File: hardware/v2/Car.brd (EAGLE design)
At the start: 83.8 x 55.9 mm, 64 parts

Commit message: Fixed PGD/PGC error (swapped) in schematic.
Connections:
- net N$28: now also ICD.5; no longer ICD.4
- net N$3: now also ICD.4; no longer ICD.5
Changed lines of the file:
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@@
 <?xml version="1.0" encoding="utf-8"?>
 <!DOCTYPE eagle SYSTEM "eagle.dtd">
-<eagle version="7.1.0">
+<eagle version="7.2.0">
 <drawing>
 <settings>
@@
 <signal name="N$3">
 <contactref element="BRAINS" pad="4"/>
-<contactref element="ICD" pad="5"/>
-<wire x1="2.032" y1="7.62" x2="38.1" y2="32.72" width="0" layer="19" extent="1-1"/>
+<contactref element="ICD" pad="4"/>
+<wire x1="1.778" y1="10.16" x2="38.1" y2="32.72" width="0" layer="19" extent="1-1"/>
 </signal>
 <signal name="N$28">
 <contactref element="BRAINS" pad="5"/>
-<contactref element="ICD" pad="4"/>
-<wire x1="1.778" y1="10.16" x2="36.83" y2="32.72" width="0" layer="19" extent="1-1"/>
+<contactref element="ICD" pad="5"/>
+<wire x1="2.032" y1="7.62" x2="36.83" y2="32.72" width="0" layer="19" extent="1-1"/>
 </signal>
 <signal name="N$30">

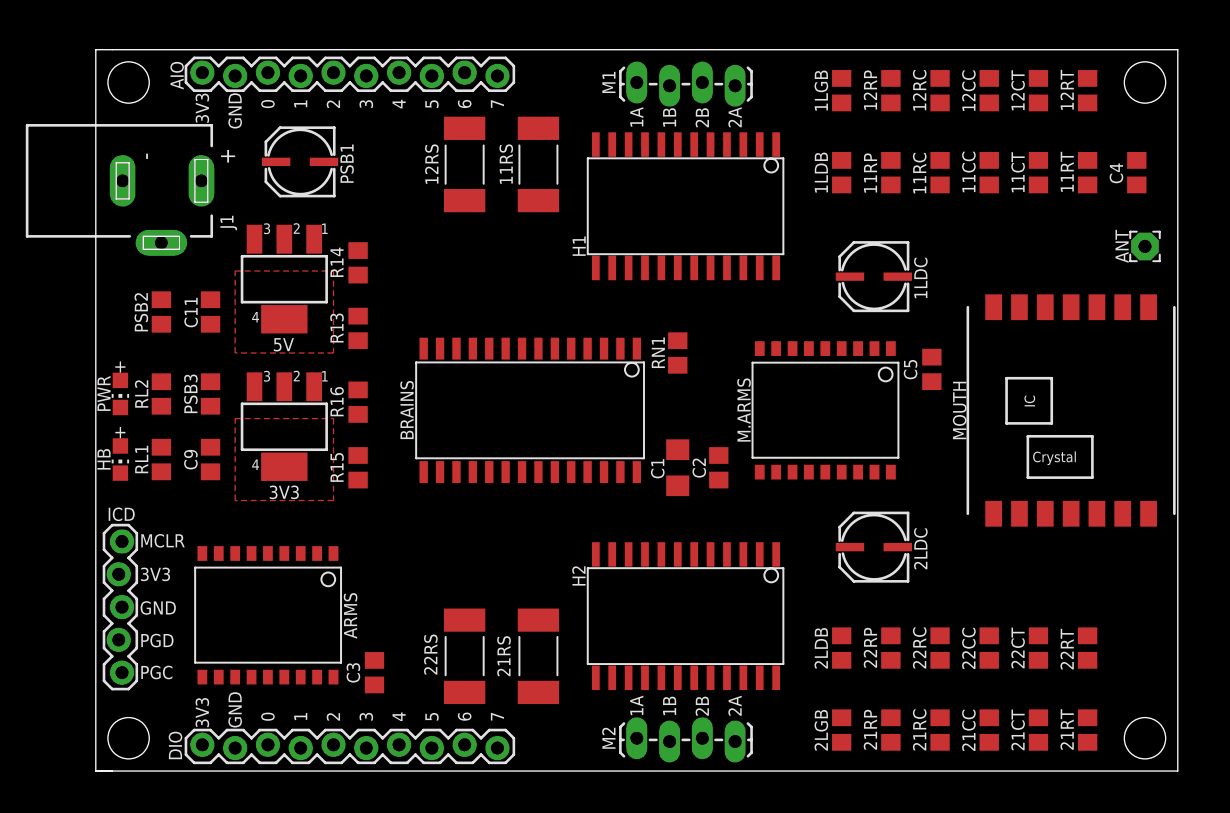
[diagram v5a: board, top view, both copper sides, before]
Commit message: Swapped non-analog input pins for ones that do support analog input. Significantly cleaned up schematic.
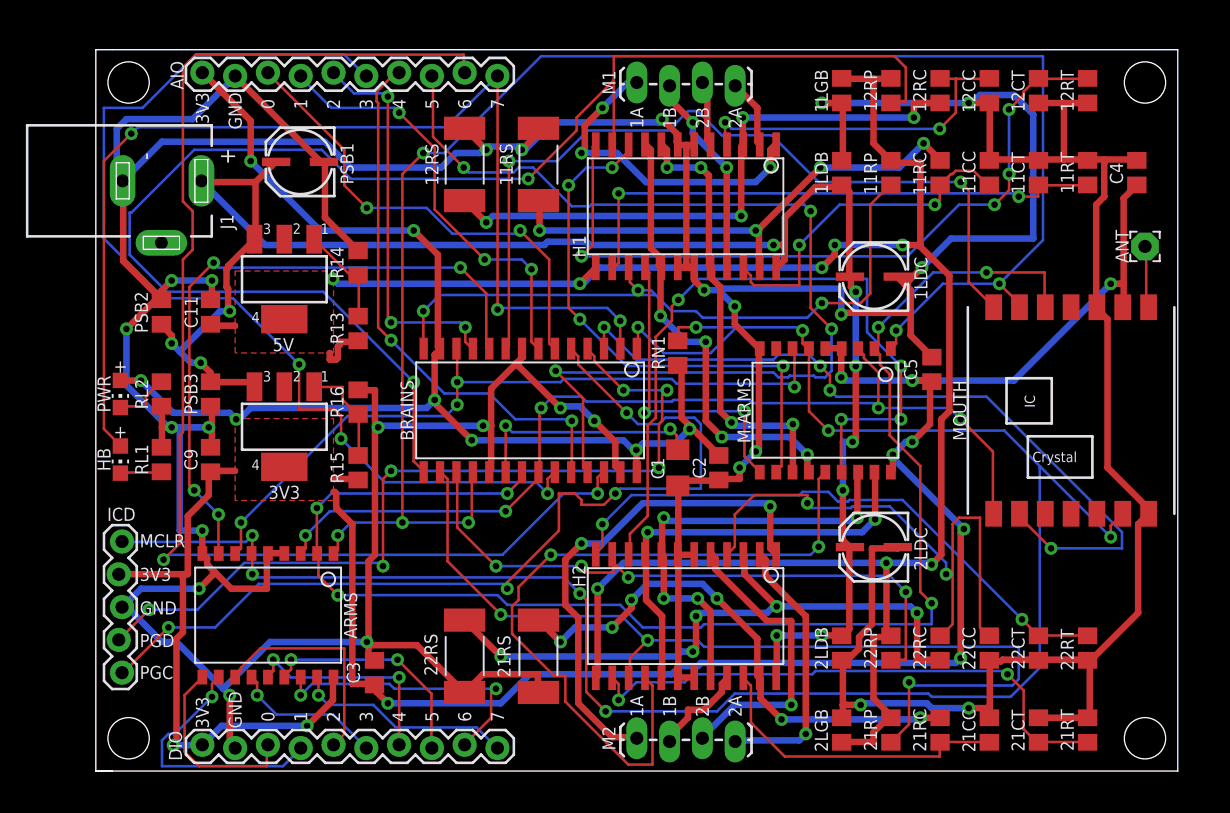
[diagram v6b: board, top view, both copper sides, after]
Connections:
- net N$12 renamed D0
- net N$19 renamed M2_V2
- net N$21 renamed M1_V2
- net N$23 renamed M1_I0X
- net N$25 renamed MOSI
- net N$26 renamed MISO
- net N$28 renamed PGC
- net N$3 renamed PGD
- net N$30 renamed M1_V1
- net N$38 renamed M2_V1
- net N$39 renamed D1
- net N$43 renamed D2
- net N$44 renamed D3
- net N$47 renamed D4
- net N$48 renamed D5
- net N$49 renamed D6
- net N$50 renamed D7
- net N$56 renamed M1_I1X
- net N$60 renamed M2_I0X
- net N$61 renamed M2_I1X
- net N$62 renamed M1_P1
- net N$63 renamed M1_P2
- net N$66 renamed M2_P1
- net N$67 renamed M2_P2
- net N$7 renamed SCLK
- net VCCIO renamed /RST
- removed net N$22: BRAINS.25, MOUTH.14
- removed net N$24: BRAINS.26, MOUTH.2
- removed net N$29: AIO.5, BRAINS.9
- removed net N$32: AIO.6, BRAINS.10
- removed net N$36: ARMS.7, BRAINS.23, M.ARMS.7
- removed net N$37: ARMS.8, BRAINS.24
- removed net N$45: AIO.3, BRAINS.2, HB.A
- removed net N$53: AIO.4, BRAINS.3
- removed net N$54: AIO.8, BRAINS.6
- removed net N$55: AIO.9, BRAINS.7
- removed net N$57: AIO.7, BRAINS.12
- removed net N$59: AIO.10, BRAINS.11
- new net A0: AIO.3, BRAINS.6
- new net A1: AIO.4, BRAINS.7
- new net A2: AIO.5, BRAINS.11
- new net A3: AIO.6, BRAINS.23
- new net A4: AIO.7, BRAINS.24
- new net A5: AIO.8, BRAINS.25
- new net A6: AIO.9, BRAINS.26
- new net A7: AIO.10, BRAINS.2, HB.A
- new net DIO_CS: ARMS.7, BRAINS.12, M.ARMS.7
- new net DIO_IRQ: ARMS.8, BRAINS.10
- new net RFM_CS: BRAINS.9, MOUTH.14
- new net RFM_IRQ: BRAINS.3, MOUTH.2
- net +3V3: now also PWR.A
- net +5V: no longer PWR.A
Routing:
- net GND: track 0.00 -> 497.1 mm, vias 0 -> 26
- net +3V3: track 0.00 -> 274.8 mm, vias 0 -> 18
- net /RST: track 0.00 -> 158.0 mm, vias 0 -> 9
- net +5V: track 0.00 -> 153.5 mm, vias 0 -> 8
- net +12V: track 0.00 -> 135.1 mm, vias 0 -> 10
- net SCLK: track 0.00 -> 129.1 mm, vias 0 -> 6
- net M1_V2: track 0.00 -> 114.6 mm, vias 0 -> 2
- net MOSI: track 0.00 -> 114.2 mm, vias 0 -> 6
- net A6: track 0.00 -> 100.6 mm, vias 0 -> 2
- net A7: track 0.00 -> 86.0 mm, vias 0 -> 3
- net A5: track 0.00 -> 80.6 mm, vias 0 -> 4
- net A3: track 0.00 -> 80.4 mm, vias 0 -> 3
- net MISO: track 0.00 -> 74.3 mm, vias 0 -> 5
- net M2_V1: track 0.00 -> 74.3 mm, vias 0 -> 3
- net PGC: track 0.00 -> 72.2 mm, vias 0 -> 4
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
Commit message: More schematic and layout cleanup.
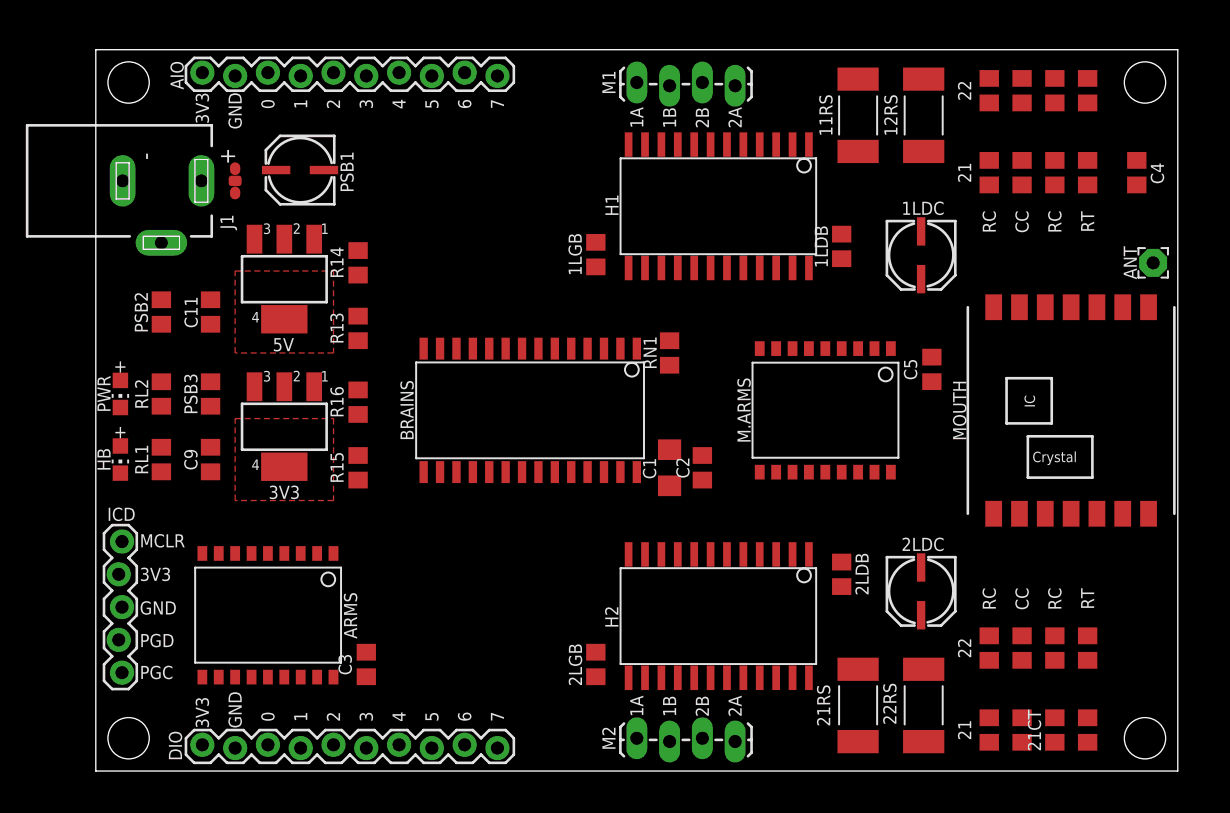
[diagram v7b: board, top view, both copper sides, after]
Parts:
- removed 11RP, 12RP, 21RP, 22RP: 10k, rcl:R0805
- added JMP1: 0R-JUMPC, jump-0r-smd:C0R-JMP
- 11CC, 11CT, 12CC, 12CT, 21CC, 21CT, 22CC, 22CT: value 820p -> 1n
- 11RC, 12RC, 21RC, 22RC: value 1k -> 2k
- 11RT, 12RT, 21RT, 22RT: value 56k -> 22k
- moved 12RS 35.8 mm to (64.1, 50.8)
- moved 22RS 35.8 mm to (64.1, 5.08)
- moved 11RS 25.1 mm to (59.1, 50.8)
- moved 21RS 25.1 mm to (59.1, 5.08)
- moved 1LGB 22.9 mm to (38.7, 40.0), turned to 90 degrees
- moved 2LGB 19.7 mm to (38.7, 8.26)
- moved 2LDB 5.71 mm to (57.8, 15.2), turned to 90 degrees
- moved 1LDB 5.71 mm to (57.8, 40.6)
- moved 2LDC 4.96 mm to (64.1, 14.0), turned to 270 degrees
- moved 1LDC 4.26 mm to (64.1, 40.0), turned to 270 degrees
- moved 11RC 3.81 mm to (69.2, 46.4)
- moved 12RC 3.81 mm to (69.2, 52.7)
- moved 21RC 3.81 mm to (69.2, 3.17)
- moved 22RC 3.81 mm to (69.2, 9.53)
- moved H1 2.54 mm to (48.3, 43.8)
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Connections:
- net +12V renamed 12V
- net +3V3 renamed 3V3
- removed net +5V: 11RP.2, 12RP.2, 1LGB.1, 21RP.2, 22RP.2, 2LGB.1, 5V.4, C11.1, H1.13, H2.13, R13.2
- new net 5V: 1LGB.1, 2LGB.1, 5V.4, C11.1, H1.13, H2.13, R13.2
- new net AGND: 11CC.2, 11CT.2, 11RS.1, 11RT.1, 12CC.2, 12CT.2, 12RS.1, 12RT.1, 1LDB.2, 1LDC.-, 21CC.2, 21CT.2, 21RS.1, 21RT.1, 22CC.2, 22CT.2, 22RS.1, 22RT.1, 2LDB.2, 2LDC.-, JMP1.3
- new net DGND: 1LGB.2, 2LGB.2, AIO.2, ARMS.4, ARMS.5, ARMS.9, BRAINS.19, BRAINS.27, BRAINS.8, C1.2, C2.2, C3.2, C4.2, C5.2, DIO.2, H1.18, H1.19, H1.6, H1.7, H2.18, H2.19, H2.6, H2.7, ICD.3, JMP1.1, M.ARMS.9, MOUTH.10, MOUTH.7, RL1.2
- net GND: now also JMP1.2; no longer 11CC.2, 11CT.2, 11RS.1, 11RT.1, 12CC.2, 12CT.2, 12RS.1, 12RT.1, 1LDB.2, 1LDC.-, 1LGB.2, 21CC.2, 21CT.2, 21RS.1, 21RT.1, 22CC.2, 22CT.2, 22RS.1, 22RT.1, 2LDB.2, 2LDC.-, 2LGB.2, AIO.2, ARMS.4, ARMS.5, ARMS.9, BRAINS.19, BRAINS.27, BRAINS.8, C1.2, C2.2, C3.2, C4.2, C5.2, DIO.2, H1.18, H1.19, H1.6, H1.7, H2.18, H2.19, H2.6, H2.7, ICD.3, M.ARMS.9, MOUTH.10, MOUTH.7, RL1.2
- net M1_V1: no longer 11RP.1
- net M1_V2: no longer 12RP.1
- net M2_V1: no longer 21RP.1
- net M2_V2: no longer 22RP.1
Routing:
- net GND: track 497.1 -> 0.00 mm, vias 26 -> 0
- net 3V3: track 274.8 -> 0.00 mm, vias 18 -> 0
- net /RST: track 158.0 -> 0.00 mm, vias 9 -> 0
- net +5V: track 153.5 -> 0.00 mm, vias 8 -> 0
- net 12V: track 135.1 -> 0.00 mm, vias 10 -> 0
- net SCLK: track 129.1 -> 0.00 mm, vias 6 -> 0
- net M1_V2: track 114.6 -> 0.00 mm, vias 2 -> 0
- net MOSI: track 114.2 -> 0.00 mm, vias 6 -> 0
- net A6: track 100.6 -> 0.00 mm, vias 2 -> 0
- net A7: track 86.0 -> 0.00 mm, vias 3 -> 0
- net A5: track 80.6 -> 0.00 mm, vias 4 -> 0
- net A3: track 80.4 -> 0.00 mm, vias 3 -> 0
- net MISO: track 74.3 -> 0.00 mm, vias 5 -> 0
- net M2_V1: track 74.3 -> 0.00 mm, vias 3 -> 0
- net PGC: track 72.2 -> 0.00 mm, vias 4 -> 0
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- added copper zone on layer 1, net +3V3
- removed copper zone on layer 1, net 3V3
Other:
- outline, holes or cut-outs redrawn
- board text added: "21"
- board text added: "22"
- board text added: "CC"
- board text added: "RC"
- board text added: "RT"

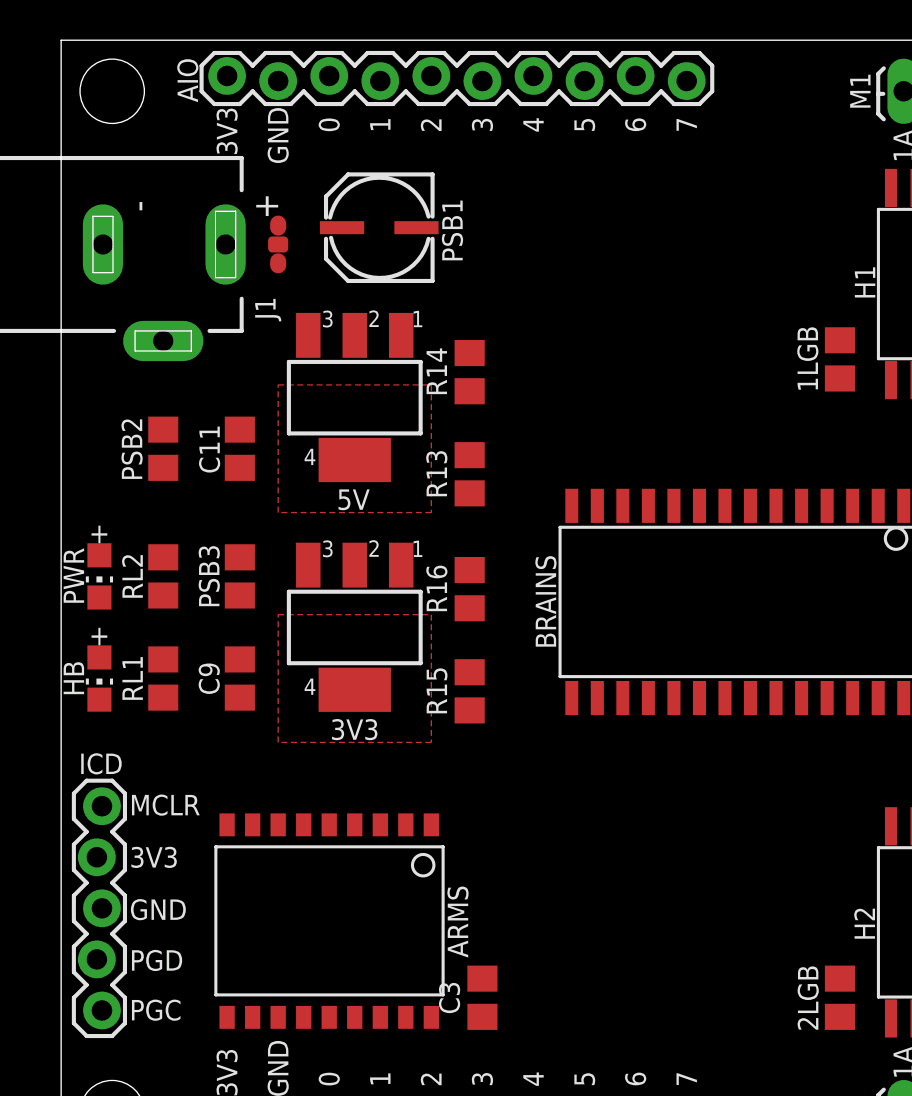
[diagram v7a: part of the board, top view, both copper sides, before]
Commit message: Adding low pass filters to PWM outputs (for motor VREF).
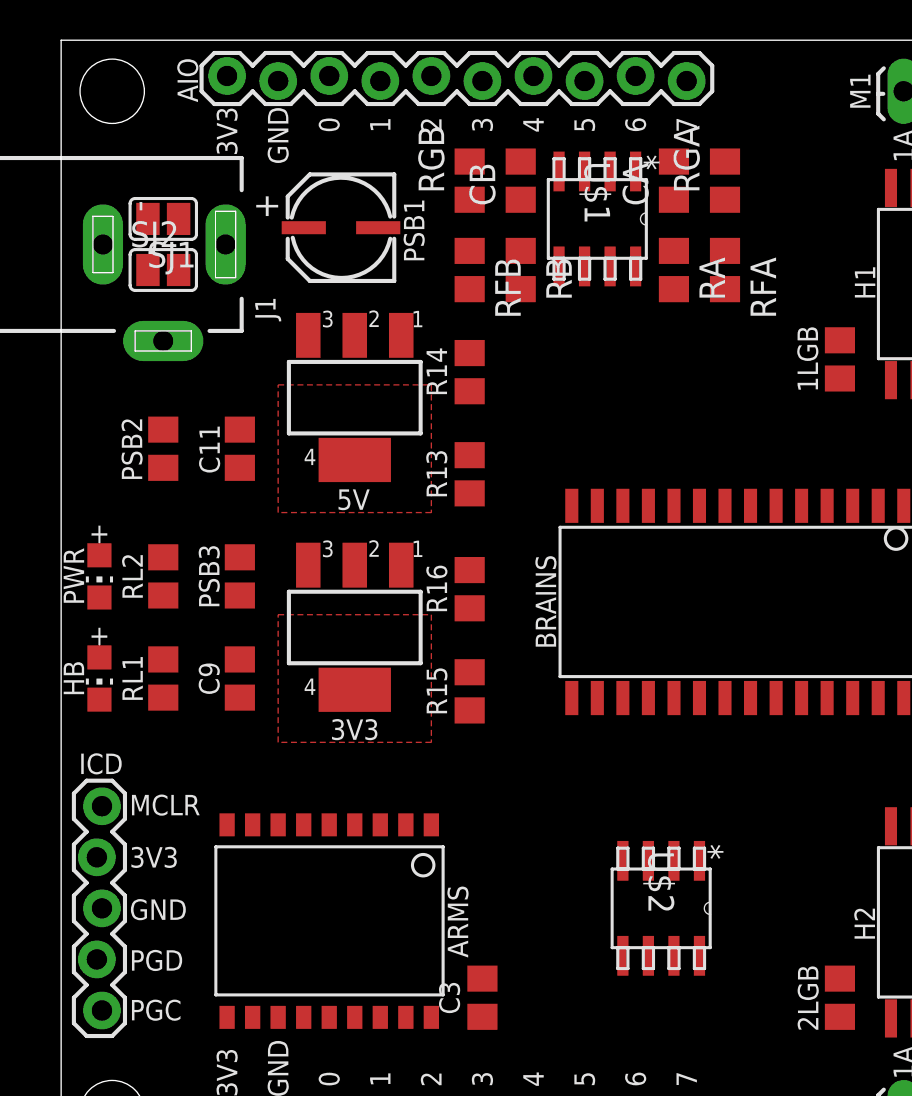
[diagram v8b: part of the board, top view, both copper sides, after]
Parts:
- removed JMP1: 0R-JUMPC, jump-0r-smd:C0R-JMP
- added CA, CB: 1n, rcl:C0805
- added RA, RB, RFA, RFB, RGA, RGB: 2k, rcl:R0805
- added SJ1, SJ2: (no value), jumper:SJ
- added U$1, U$2: MCP6L2-X_SN, microchip2:SOIC8-N_MC
- moved PSB1 1.90 mm to (14.0, 46.4)
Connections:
- new net M1_PWM1: BRAINS.14, RA.2
- new net M1_PWM2: BRAINS.15, RB.2
- new net M2_PWM1: BRAINS.16
- new net M2_PWM2: BRAINS.17
- new net N$21: RFB.2, U$1.6
- new net N$22: CB.1, RB.1, U$1.5
- new net N$3: CA.1, RA.1, U$1.3
- new net N$7: RFA.2, U$1.2
- new net VDD: U$2.8
- new net VSS: U$2.4
- net 5V: now also U$1.8
- net AGND: now also CA.2, CB.2, RGA.2, RGB.2, SJ1.1, U$1.4; no longer JMP1.3
- net DGND: now also SJ2.2; no longer JMP1.1
- net GND: now also SJ1.2, SJ2.1; no longer JMP1.2
- net M1_V1: now also RFA.1, RGA.1, U$1.1; no longer BRAINS.14
- net M1_V2: now also RFB.1, RGB.1, U$1.7; no longer BRAINS.15
- net M2_V1: no longer BRAINS.16
- net M2_V2: no longer BRAINS.17
